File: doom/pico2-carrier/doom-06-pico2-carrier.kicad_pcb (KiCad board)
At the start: 2 copper layers, 160 x 100 mm, 62 parts, among them J1 SJ1-3525N, Q1 AO3401A, Q2 FS8205A, SW1 PTS645SM43SMTR92 LFS, SW10 PTS645SM43SMTR92 LFS, SW11 MSK12C02, SW2 PTS645SM43SMTR92 LFS, SW3 PTS645SM43SMTR92 LFS, SW4 PTS645SM43SMTR92 LFS, SW5 PTS645SM43SMTR92 LFS, SW6 PTS645SM43SMTR92 LFS, SW7 PTS645SM43SMTR92 LFS, SW8 PTS645SM43SMTR92 LFS, SW9 PTS645SM43SMTR92 LFS, U1 SC1631, U2 PCM5102APWR, U3 DW01A, U4 BQ24075RGTR

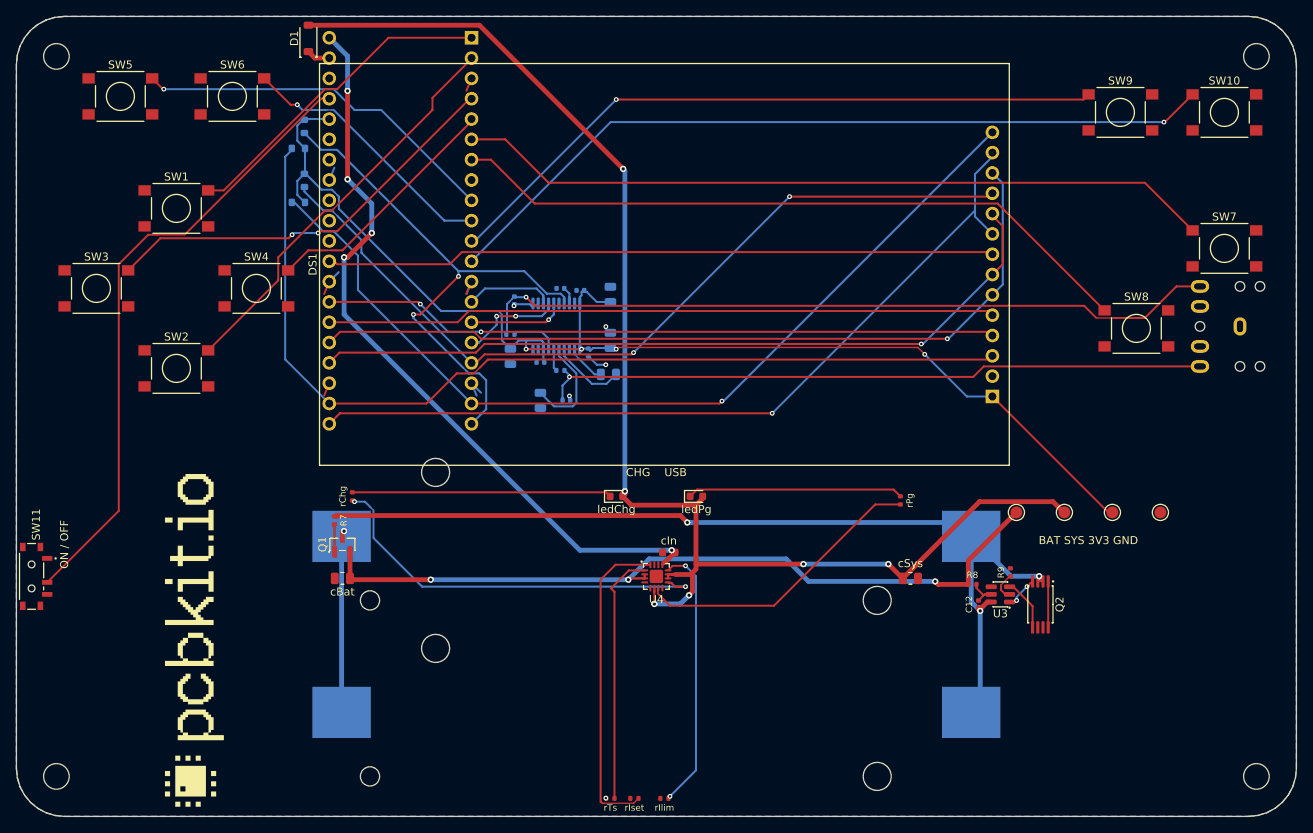
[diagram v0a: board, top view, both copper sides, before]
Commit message: Boards pass check and KiCad 10's DRC again: holes in courtyards, the USB net rename
pcbkit's check now has KiCad 10's pth/npth_inside_courtyard (pcbkit be5b6955), and 13 boards
failed it. KiCad's own DRC (kicad-cli 10) reports the same holes on every one of them.

- Parts that really stand above the holes under them (a screen or a Nano on its sockets, the
  Delta-S02's КМ-6 capacitors flat under its chips, as the factory placed them): a courtyard rule
  for the pair, written to each board's .kicad_dru, so KiCad's DRC agrees.
- Real collisions moved: servo-controller's dial 3 mm up (the Nano's socket pins came out under
  it), c3-pocket's fourth M3 hole from under a cell holder to the top edge's middle, s3-rgb's
  D-pad 2 mm up (a holder's peg came through under the down key).
- v003-emu, c3-pocket, rp2040-tft, rp2350-psram, s3-rgb, teensy41: re-routed for the standard USB
  block's renamed net (usb/raw is usb/vbusIn since pcbkit 2088839e): their tracks still carried
  the old name and shorted the fuse and connector pads.
- p4-touch-7: its board file still had a courtyard for the panel the design gives none (KiCad
  reported 114 courtyard errors); written again.

Measured on the dev host: all 44 registry boards `pcbkit check` complete with 0 errors, and
kicad-cli pcb drc 0 errors on every board.

Claude-Session: https://claude.ai/code/session_018URVYF1YPgyrMNetY9yT1T
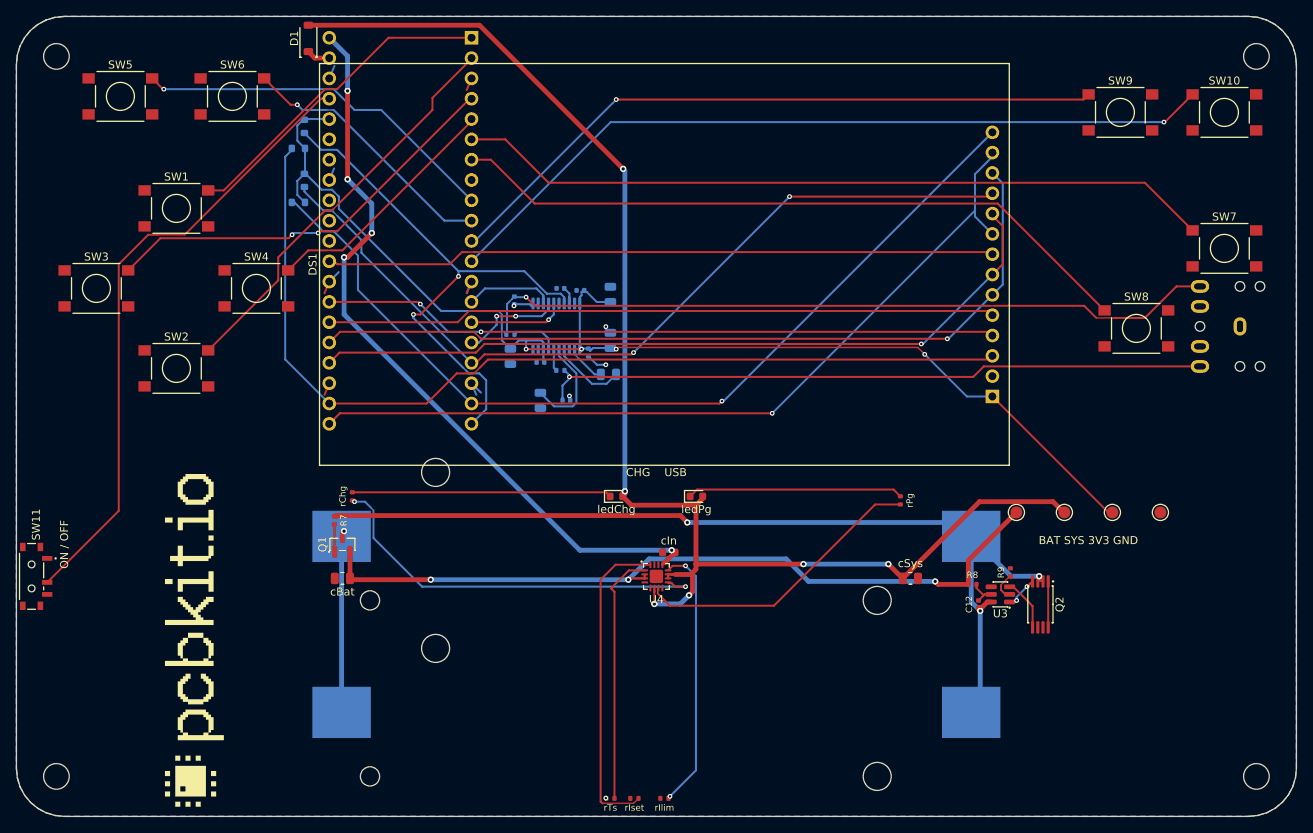
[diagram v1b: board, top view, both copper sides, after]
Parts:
- H1, H2, H3, H4: value (none) -> MountingHole_3.2mm_M3
- U1: value SC1631 -> PIM724; footprint Raspberry_Pi_Pico_2_Socket_2x20_P2.54mm_W17.78mm -> Pimoroni_Pico_Plus_2_Socket_2x20_P2.54mm_W17.78mm
- logo: value (none) -> Logo_PCBKit_pcbkit.io
- tpBat, tpGnd, tpSys, tpV3: value (none) -> TestPoint_Round_D1.5mm
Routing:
- net GND: track 23.0 -> 24.2 mm

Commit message: doom: a resettable fuse per 18650 cell, a 2 % backlight clamp, a 1 A LDO on the S3 boards
The verifier (wiring-parallel-cells) found the two holders of every Doom board directly in parallel:
a cell put in backwards, or one much fuller than the other, drives the other through nothing but
the cells' resistance (about 56-168 A). Each holder's + now reaches BAT_IN through its own 2 A
resettable fuse (Littelfuse 1812L200/16GR, C18198340: 16 V, 100 A interrupting) on new nets
CELL1_P / CELL2_P. Nothing else moved; the boards were re-routed for the new nets.

- s3-rgb: the MT3608 backlight's open-panel clamp was a 28 V 5 % zener (bound 30.0 V against the
  switch's 30 V). It is now two 2 % zeners in series, UDZVTE-1718B + UDZVTE-1710B (27.33-28.56 V;
  LCSC stocks no single 28 V 2 % part). That is under 29.2 V and above the panel's 27.2 V.
- s3-rgb, s3-handheld: TLV75533 (500 mA) -> TLV75733 (1 A, C485517, same DBV pins; sheet from
  SBVS322C), for the ESP32-S3's 500 mA supply peaks (erc-supply-peak).
- c3-pocket, v003-emu: the USB PTC's hold is 750 mA, as the part (nSMD075) is (rating-current).
- pico2-carrier: the CHG/PG LEDs 1.5 mm further from the display's courtyard. rp2350-handheld:
  the logo off the LCD's courtyard and BT1's peg.
- READMEs: the per-cell fuses, the boards already ordered (s3-rgb, JLC W2026102705013253: insert
  the cells one at a time), status and BOM as check and the fab export give them now.

Measured on the dev host (pcbkit 5e0d2cc8): all 11 complete, 0 errors, 0 unrouted. What is left is
erc-rail-name (sent to the verifier as false positives) and full-speed USB pair coupling. The MCU
pins' nets are unchanged on every board, so the firmware and its simulation are unchanged.

Claude-Session: https://claude.ai/code/session_01B3VRfBCg9vAvGVWujVGarr
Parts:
- added F1: PTC 2000mA, Fuse_1812_4532Metric, B.Cu at (133.5, 179.8)
- added F2: PTC 2000mA, Fuse_1812_4532Metric, B.Cu at (134.8, 170.2)
- moved ledChg 3.50 mm to (175.0, 163.5)
- moved ledPg 3.50 mm to (185.0, 163.5)
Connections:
- BT1 pad 2: BAT_IN -> CELL1_P
- BT2 pad 2: BAT_IN -> CELL2_P
- SW1 pad 2: UP -> GND
- SW10 pad 2: ENTER -> GND
- SW2 pad 2: DOWN -> GND
- SW3 pad 2: LEFT -> GND
- SW4 pad 2: RIGHT -> GND
- SW5 pad 2: STRAFE_L -> GND
- SW6 pad 2: STRAFE_R -> GND
- SW7 pad 2: FIRE -> GND
- SW8 pad 2: USE -> GND
- SW9 pad 2: MENU -> GND
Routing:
- net CELL1_P: track 0.00 -> 9.27 mm
- net BAT_IN: track 22.0 -> 14.7 mm
- net CELL2_P: track 0.00 -> 7.19 mm
- net SYS: track 173.1 -> 178.7 mm, vias 6 -> 4
- net CHG_LED: track 32.4 -> 33.9 mm
- net PG_LED: track 27.0 -> 27.7 mm

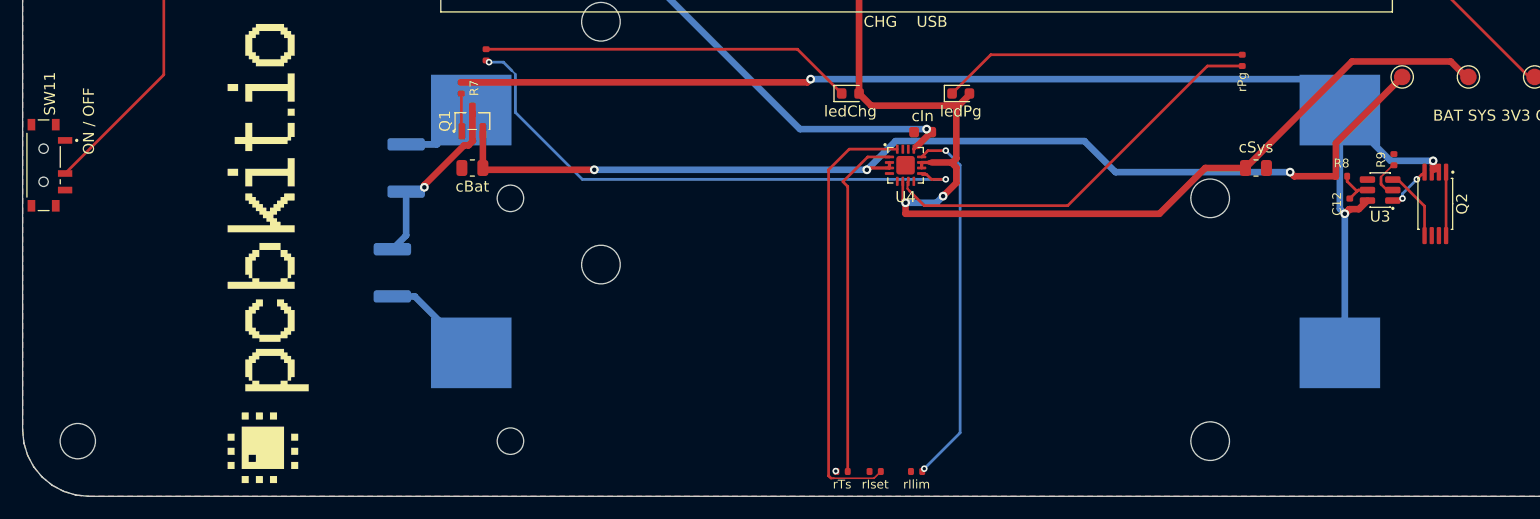
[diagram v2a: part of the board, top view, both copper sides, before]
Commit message: boards: 15 boards rebuilt on pcbkit 20ffacdc9 (their pours under the 0.25 mm hole clearance)
Every board checked with main: 17 of 44 failed on hole-clearance (pours filled before fill c6 made
0.25 mm KiCad's hole clearance the default), keepout (holes now sized by the board) or
place-corner. design.run {} on each (placement and routing kept, pours refilled): 15 now complete,
0 errors. Not here: esp32-p4-touch-lcd-7b and p4-touch-7 (a build reroutes their pairs: 21 and 7
unrouted; kept as they were, 2,372 and 919 hole-clearance errors: a refill without a reroute is
needed).

Claude-Session: https://claude.ai/code/session_01BAgp959tApA8aEg85EYgfb
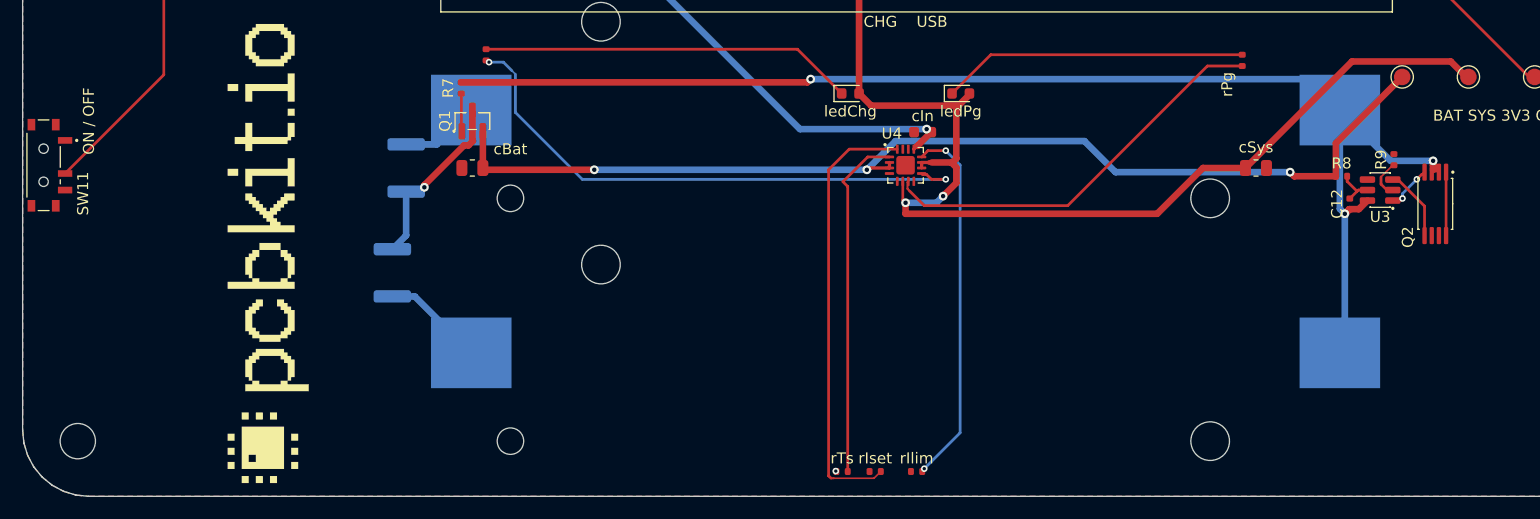
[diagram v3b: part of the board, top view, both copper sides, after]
